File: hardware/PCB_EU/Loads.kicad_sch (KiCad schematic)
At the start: 15 parts, among them J701 PTC + / RETURN, J702 PUMP + / RETURN, Q701 BC847B-DIO, Q702 BC857B, Q703 IRF1010ESPBF, Q704 AO3422

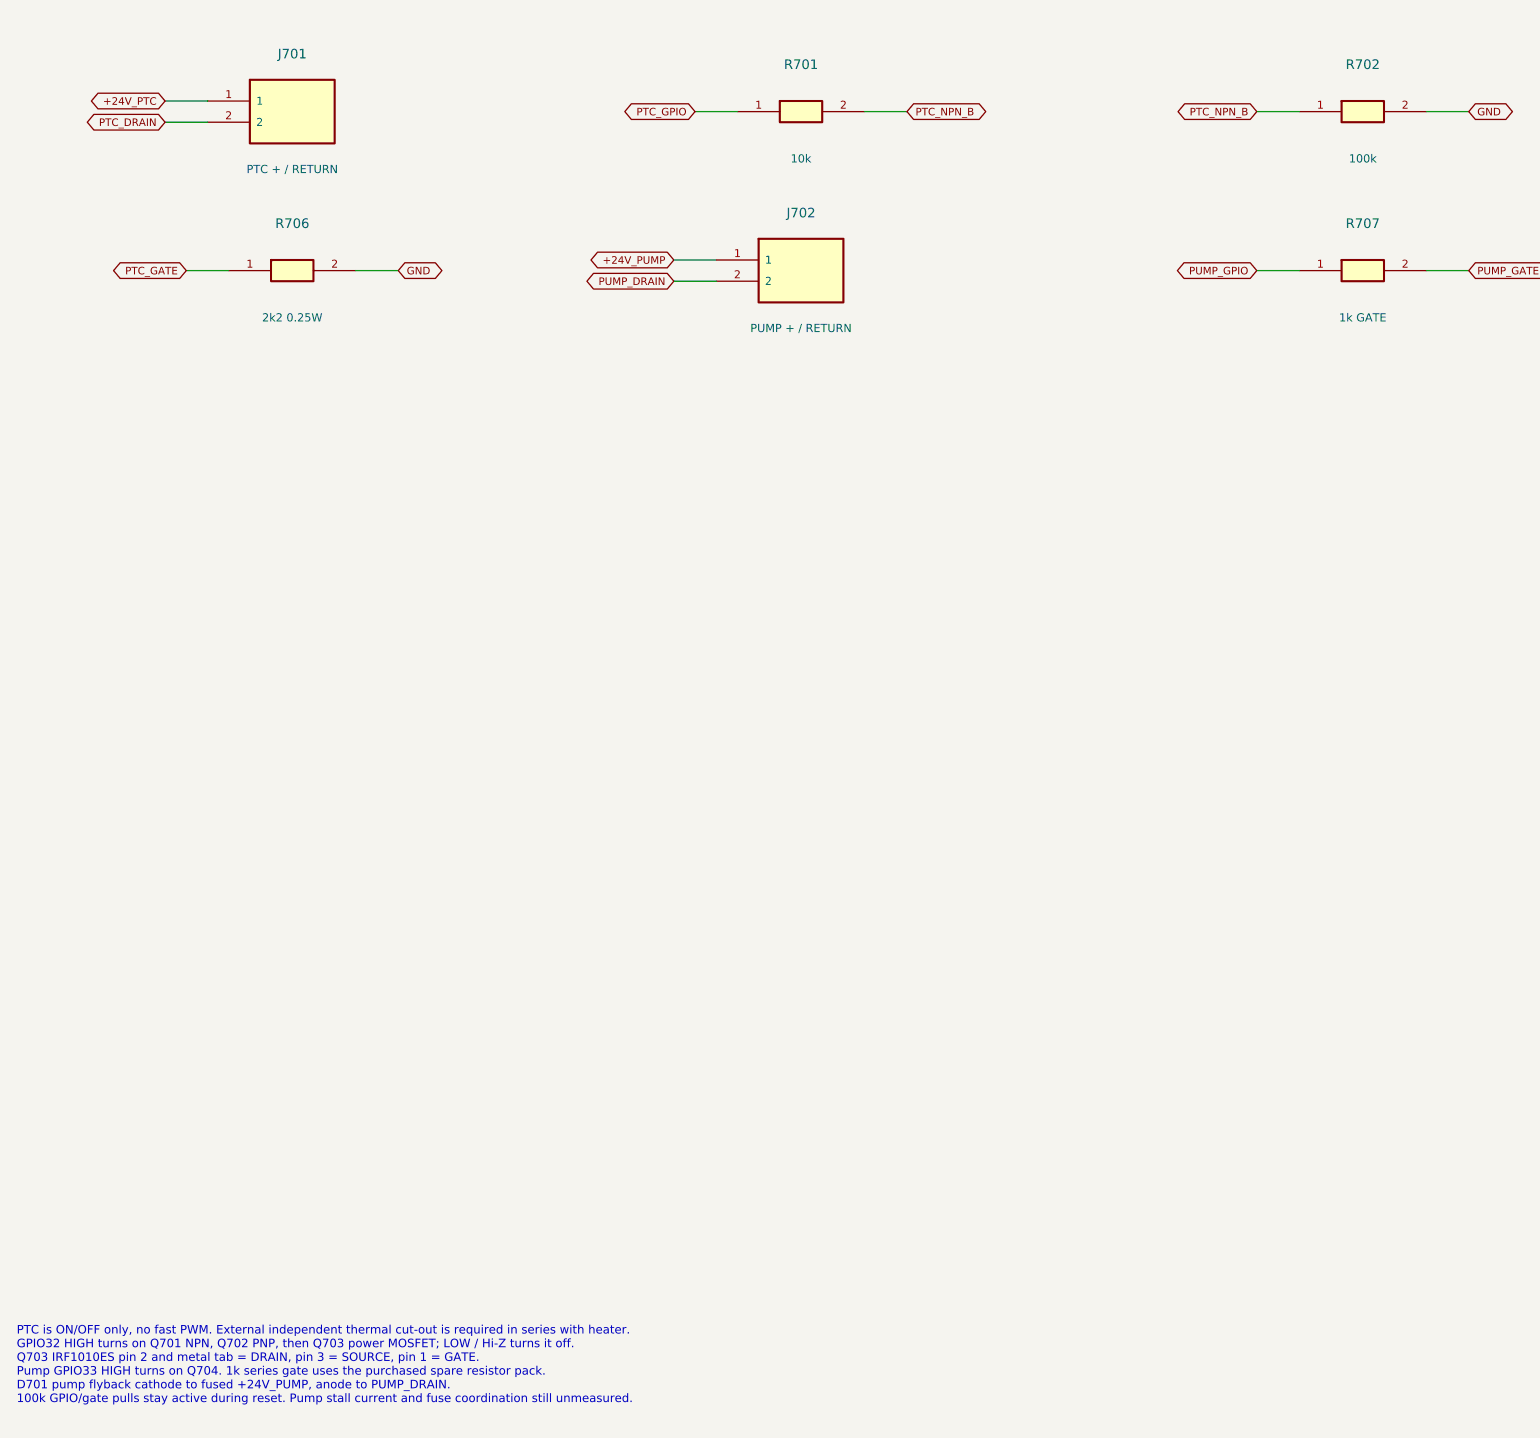
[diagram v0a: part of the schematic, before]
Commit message: hardware: apply PCB_EU review fixes
- R702 100k -> 4k7: ESP32 internal pull-up on GPIO32 (old firmware
  INPUT_PULLUP) could switch the 100 W PTC on.
- C208 100n -> 1u for the Espressif EN delay.
- Remove TC4427A driver and its parts; each LM3429 GATE drives its own
  IRF540Z through 4R7 (driver was 20-25 mm from both MOSFETs).
- Add reverse-polarity protection: Q102 IRF1010ES in the input return
  with a 5k6+5k6 / 10k gate divider.
- F103 label: UST 1206 is time-lag.
- Rebuild PCB via build_board.py + route_power.py, rerun all checks on
  KiCad 10.0.7: ERC 0, DRC 0 / parity 0, 355 unrouted, 51 checks.
- Parts estimate 80.00 -> 78.59 EUR; check ceiling raised to 100 EUR.

Co-Authored-By: Claude Opus 5.5 (1M context) <noreply@anthropic.com>
Claude-Session: https://claude.ai/code/session_01AxccZX6Cb4FnRKJMrFYMSX
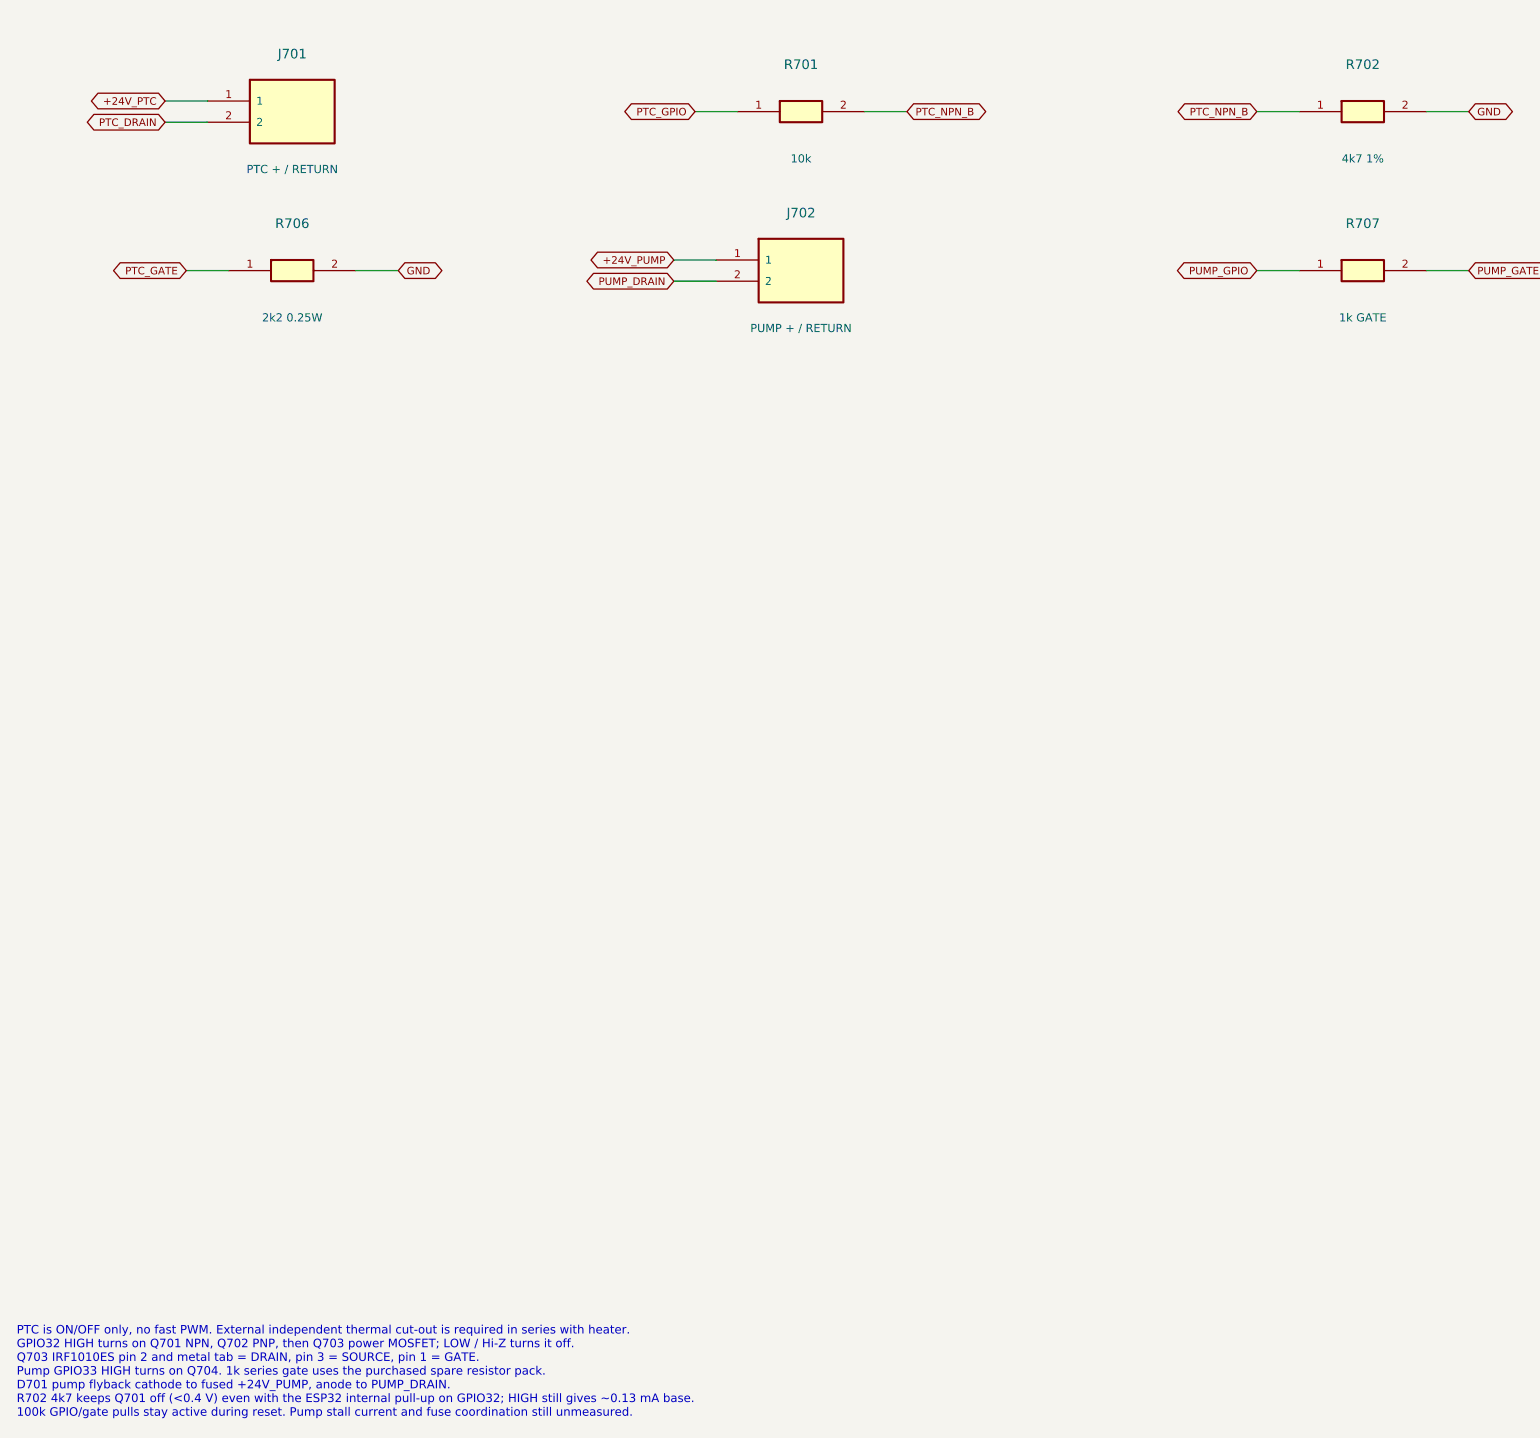
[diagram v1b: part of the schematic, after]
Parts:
- R702: value 100k -> 4k7 1%; footprint Resistor_SMD:R_0603_1608Metric -> Resistor_SMD:R_1206_3216Metric; MPN SMD0603-100K -> SMD1206 4K7 1%
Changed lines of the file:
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@@
 (kicad_sch (version 20260306) (generator "eeschema") (generator_version "10.0") (paper "A3") (title_block (title "07 | PTC heater and 24 V pump") (date "2026-10-20") (rev "EU-0.1") (company "GrowBox | EU prototype") (comment 1 "SCHEMATIC DRAFT | PARTIAL LED1 PCB ROUTING | no manufacturing release"))
 (text "07 | PTC heater and 24 V pump" (at 12.7 12.7 0) (effects (font (size 2 2)) (justify left top)))
-(text "PTC is ON/OFF only, no fast PWM. External independent thermal cut-out is required in series with heater.\nGPIO32 HIGH turns on Q701 NPN, Q702 PNP, then Q703 power MOSFET; LOW / Hi-Z turns it off.\nQ703 IRF1010ES pin 2 and metal tab = DRAIN, pin 3 = SOURCE, pin 1 = GATE.\nPump GPIO33 HIGH turns on Q704. 1k series gate uses the purchased spare resistor pack.\nD701 pump flyback cathode to fused +24V_PUMP, anode to PUMP_DRAIN.\n100k GPIO/gate pulls stay active during reset. Pump stall current and fuse coordination still unmeasured." (at 12.7 251 0) (effects (font (size 1.02 1.02)) (justify left top)))
+(text "PTC is ON/OFF only, no fast PWM. External independent thermal cut-out is required in series with heater.\nGPIO32 HIGH turns on Q701 NPN, Q702 PNP, then Q703 power MOSFET; LOW / Hi-Z turns it off.\nQ703 IRF1010ES pin 2 and metal tab = DRAIN, pin 3 = SOURCE, pin 1 = GATE.\nPump GPIO33 HIGH turns on Q704. 1k series gate uses the purchased spare resistor pack.\nD701 pump flyback cathode to fused +24V_PUMP, anode to PUMP_DRAIN.\nR702 4k7 keeps Q701 off (<0.4 V) even with the ESP32 internal pull-up on GPIO32; HIGH still gives ~0.13 mA base.\n100k GPIO/gate pulls stay active during reset. Pump stall current and fuse coordination still unmeasured." (at 12.7 251 0) (effects (font (size 1.02 1.02)) (justify left top)))
 (symbol (lib_id "EU:J2") (at 45.72 105.41 0) (unit 1) (in_bom yes) (on_board yes) (dnp no)
 (property "Reference" "J701" (at 45.72 98.5 0) (effects (font (size 1.15 1.15)) ))
@@
 (symbol (lib_id "EU:R") (at 173.99 105.41 0) (unit 1) (in_bom yes) (on_board yes) (dnp no)
 (property "Reference" "R702" (at 173.99 99.77 0) (effects (font (size 1.15 1.15)) ))
-(property "Value" "100k" (at 173.99 111.05 0) (effects (font (size 0.98 0.98)) ))
-(property "Footprint" "Resistor_SMD:R_0603_1608Metric" (at 173.99 105.41 0) (effects (font (size 1 1)) (hide yes)))
+(property "Value" "4k7 1%" (at 173.99 111.05 0) (effects (font (size 0.98 0.98)) ))
+(property "Footprint" "Resistor_SMD:R_1206_3216Metric" (at 173.99 105.41 0) (effects (font (size 1 1)) (hide yes)))
 (property "Datasheet" "" (at 173.99 105.41 0) (effects (font (size 1 1)) (hide yes)))
-(property "MPN" "SMD0603-100K" (at 173.99 105.41 0) (effects (font (size 1 1)) (hide yes)))
+(property "MPN" "SMD1206 4K7 1%" (at 173.99 105.41 0) (effects (font (size 1 1)) (hide yes)))
 (property "Design_note" "" (at 173.99 105.41 0) (effects (font (size 1 1)) (hide yes)))
 (property "FootprintStatus" "PACKAGE ONLY - verify before PCB" (at 173.99 105.41 0) (effects (font (size 1 1)) (hide yes)))

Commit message: PCB_EU: all terminals at the board edges, no HS2, fans on KF2510-4A, SHT4x on XH2.54-4P-90
Per Igors (22.10.2026):
- stack stated as 1 oz outer / 0.5 oz inner in DESIGN.md;
- heatsink HS2 removed from the LED2 channel (Q601 runs without a heatsink,
  about 54 C rise, to be measured on the prototype), freed area used for the
  pump terminal J702 and its parts at the right edge;
- J101, J201, J411, J421, J401, J403, J701, J702 moved so that every cable
  entry faces the board edge; J701 changed from DG301R to DG306;
- fan connectors J411/J421 are 4-pin KF2510-4A headers (Molex KK-254
  footprint), J412/J422 removed;
- SHT4x on one right-angle XH2.54-4P-90 header J401 (JST XH S4B-XH-A
  footprint), J402 removed;
- input, trunk and PTC copper re-routed in routing.json; the F101.2 trunk
  now starts with a 2.4 mm neck inside the pad (it was not attached before);
- BOM: quantities and total (82.50 EUR) unchanged, the new rows have no shop
  or price and are flagged for the BOM review.

Checks (KiCad 10.0.7): ERC 0, 56 connectivity checks, 22639 placement checks,
DRC 0 / parity 0 / unconnected 0, rebuild from the repository is byte-identical.
ampacity.py: worst IPC-2221 rise 38 C, three vias above the 2 A rule of thumb.

Co-Authored-By: Claude Sonnet 5.5 <noreply@anthropic.com>
Claude-Session: https://claude.ai/code/session_01AxccZX6Cb4FnRKJMrFYMSX
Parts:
- J701: footprint EU_Mechanical:TerminalBlock_Degson_DG301R-5.0_1x02 -> EU_Mechanical:TerminalBlock_Degson_DG306-5.0_1x02; Design_note (none) -> Bottom-edge DG306 since 2026-10-22: 15 A / 1.5 mm2 rating c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; MPN DG301R-5.0-2P12 -> DG306-5.0-2P12
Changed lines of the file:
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@@
 (property "Reference" "J701" (at 45.72 98.5 0) (effects (font (size 1.15 1.15)) ))
 (property "Value" "PTC + / RETURN" (at 45.72 112.32 0) (effects (font (size 0.98 0.98)) ))
-(property "Footprint" "EU_Mechanical:TerminalBlock_Degson_DG301R-5.0_1x02" (at 45.72 105.41 0) (effects (font (size 1 1)) (hide yes)))
+(property "Footprint" "EU_Mechanical:TerminalBlock_Degson_DG306-5.0_1x02" (at 45.72 105.41 0) (effects (font (size 1 1)) (hide yes)))
 (property "Datasheet" "" (at 45.72 105.41 0) (effects (font (size 1 1)) (hide yes)))
-(property "MPN" "DG301R-5.0-2P12" (at 45.72 105.41 0) (effects (font (size 1 1)) (hide yes)))
-(property "Design_note" "" (at 45.72 105.41 0) (effects (font (size 1 1)) (hide yes)))
+(property "MPN" "DG306-5.0-2P12" (at 45.72 105.41 0) (effects (font (size 1 1)) (hide yes)))
+(property "Design_note" "Bottom-edge DG306 since 2026-10-22: 15 A / 1.5 mm2 rating covers the 4.5 A heater" (at 45.72 105.41 0) (effects (font (size 1 1)) (hide yes)))
 (property "FootprintStatus" "DRAWING CHECKED - physical fit and PCB validation pending" (at 45.72 105.41 0) (effects (font (size 1 1)) (hide yes)))
 (pin "1")
